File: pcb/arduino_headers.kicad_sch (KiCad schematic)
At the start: 4 parts, among them J4 Conn_01x08_Pin, J5 Conn_01x10_Pin, J6 Conn_01x06_Pin, J7 Conn_01x08_Pin

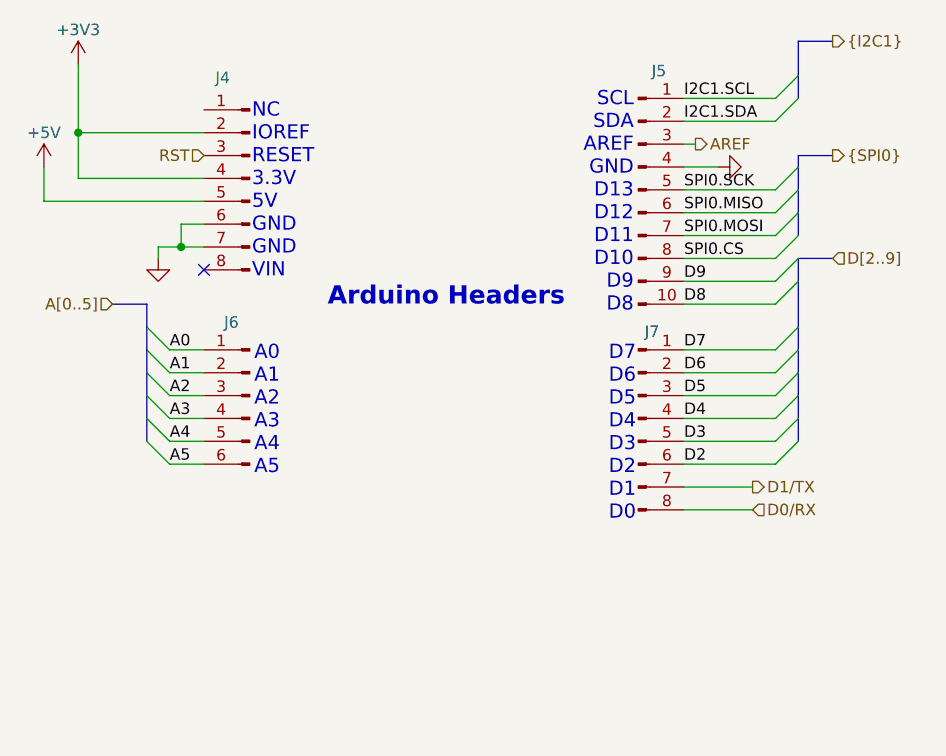
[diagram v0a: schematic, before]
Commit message: Added gerbers, added 2x3 Arduino header.
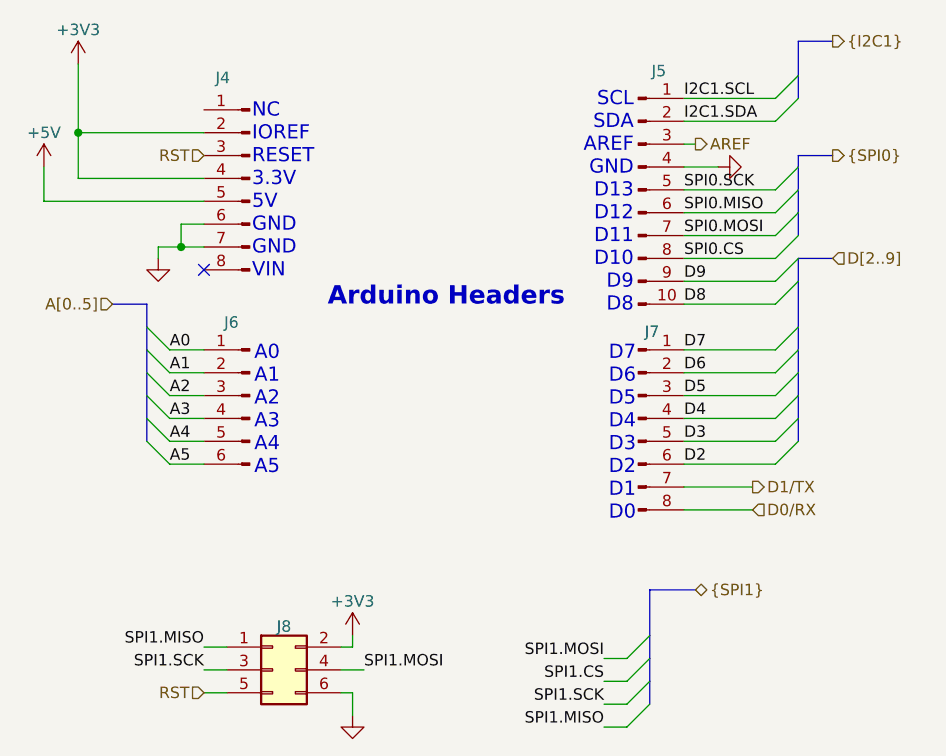
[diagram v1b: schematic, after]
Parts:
- added J8: Conn_02x03_Odd_Even, Connector_PinSocket_2.54mm:PinSocket_2x03_P2.54mm_Vertical, symbol Connector_Generic:Conn_02x03_Odd_Even
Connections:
- net +3V3: now also J8.2 (Pin_2)
- net GND: now also J8.6 (Pin_6)
- net RST: now also J8.5 (Pin_5)
- new net SPI1.MISO: J8.1 (Pin_1)
- new net SPI1.MOSI: J8.4 (Pin_4)
- new net SPI1.SCK: J8.3 (Pin_3)

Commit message: Added remaining part numbers, removed silk for holes, minor touchups
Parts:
- J4, J7: MPN (none) -> NPTC081KFXC-RC
- J5: MPN (none) -> NPTC101KFXC-RC
- J6: MPN (none) -> NPTC061KFXC-RC
- J8: footprint Connector_PinSocket_2.54mm:PinSocket_2x03_P2.54mm_Vertical -> Connector_PinHeader_2.54mm:PinHeader_2x03_P2.54mm_Vertical; MPN (none) -> 67997-206HLF
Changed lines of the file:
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@@
+			)
+		)
+		(property "MPN" "NPTC101KFXC-RC"
+			(at 177.8 82.55 0)
+			(effects
+				(font
+					(size 1.27 1.27)
+				)
+				(hide yes)
 			)
 		)
@@
 			)
 		)
+		(property "MPN" "NPTC081KFXC-RC"
+			(at 134.62 81.28 0)
+			(effects
+				(font
+					(size 1.27 1.27)
+				)
+				(hide yes)
+			)
+		)
 		(pin "2"
 		)
@@
 			)
 		)
+		(property "MPN" "NPTC061KFXC-RC"
+			(at 134.62 105.41 0)
+			(effects
+				(font
+					(size 1.27 1.27)
+				)
+				(hide yes)
+			)
+		)
 		(pin "6"
 		)
@@
 			)
 		)
-		(property "Footprint" "Connector_PinSocket_2.54mm:PinSocket_2x03_P2.54mm_Vertical"
+		(property "Footprint" "Connector_PinHeader_2.54mm:PinHeader_2x03_P2.54mm_Vertical"
 			(at 137.16 135.89 0)
 			(effects
@@
 			)
 		)
+		(property "MPN" "67997-206HLF"
+			(at 137.16 135.89 0)
+			(effects
+				(font
+					(size 1.27 1.27)
+				)
+				(hide yes)
+			)
+		)
 		(pin "1"
 		)
@@
 			(at 177.8 107.95 0)
 			(effects
+				(font
+					(size 1.27 1.27)
+				)
+				(hide yes)
+			)
+		)
+		(property "MPN" "NPTC081KFXC-RC"
+			(at 177.8 107.95 0)
+			(effects

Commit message: R0.1 released
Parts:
- renumbered J4 to J5, J5 to J6, J6 to J7, J7 to J8, J8 to J9
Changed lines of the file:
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@@
 		(on_board yes)
 		(dnp no)
-		(property "Reference" "J5"
+		(property "Reference" "J6"
 			(at 180.086 69.342 0)
 			(effects
@@
 			(project "blocky_breakout_pcb"
 				(path "/deaf739e-0e27-4f2f-890a-6dd284a38e9f/7c88a4ba-9535-4e16-9d9d-21b16df8d31a"
-					(reference "J5")
+					(reference "J6")
 					(unit 1)
 				)
@@
 		(on_board yes)
 		(dnp no)
-		(property "Reference" "#PWR048"
+		(property "Reference" "#PWR055"
 			(at 111.76 83.82 0)
 			(effects
@@
 			(project ""
 				(path "/deaf739e-0e27-4f2f-890a-6dd284a38e9f/7c88a4ba-9535-4e16-9d9d-21b16df8d31a"
-					(reference "#PWR048")
+					(reference "#PWR055")
 					(unit 1)
 				)
@@
 		(dnp no)
 		(fields_autoplaced yes)
-		(property "Reference" "#PWR067"
+		(property "Reference" "#PWR059"
 			(at 146.05 147.32 0)
 			(effects
@@
 			(project "blocky_breakout_pcb"
 				(path "/deaf739e-0e27-4f2f-890a-6dd284a38e9f/7c88a4ba-9535-4e16-9d9d-21b16df8d31a"
-					(reference "#PWR067")
+					(reference "#PWR059")
 					(unit 1)
 				)
@@
 		(on_board yes)
 		(dnp no)
-		(property "Reference" "J4"
+		(property "Reference" "J5"
 			(at 130.81 70.104 0)
 			(effects
@@
 			(project "blocky_breakout_pcb"
 				(path "/deaf739e-0e27-4f2f-890a-6dd284a38e9f/7c88a4ba-9535-4e16-9d9d-21b16df8d31a"
-					(reference "J4")
+					(reference "J5")
 					(unit 1)
 				)
@@
 		(dnp no)
 		(fields_autoplaced yes)
-		(property "Reference" "#PWR049"
+		(property "Reference" "#PWR056"
 			(at 193.04 80.01 0)
 			(effects
@@
 			(project "blocky_breakout_pcb"
 				(path "/deaf739e-0e27-4f2f-890a-6dd284a38e9f/7c88a4ba-9535-4e16-9d9d-21b16df8d31a"
-					(reference "#PWR049")
+					(reference "#PWR056")
 					(unit 1)
 				)
@@
 		(on_board yes)
 		(dnp no)
-		(property "Reference" "J6"
+		(property "Reference" "J7"
 			(at 132.588 97.282 0)
 			(effects
@@
 			(project "blocky_breakout_pcb"
 				(path "/deaf739e-0e27-4f2f-890a-6dd284a38e9f/7c88a4ba-9535-4e16-9d9d-21b16df8d31a"
-					(reference "J6")
+					(reference "J7")
 					(unit 1)
 				)
@@
 		(on_board yes)
 		(dnp no)
-		(property "Reference" "J8"
+		(property "Reference" "J9"
 			(at 138.43 131.064 0)
 			(effects
@@
 			(project ""
 				(path "/deaf739e-0e27-4f2f-890a-6dd284a38e9f/7c88a4ba-9535-4e16-9d9d-21b16df8d31a"
-					(reference "J8")
+					(reference "J9")
 					(unit 1)
 				)
@@
 		(on_board yes)
 		(dnp no)
-		(property "Reference" "J7"
+		(property "Reference" "J8"
 			(at 179.324 98.298 0)
 			(effects
@@
 			(project "blocky_breakout_pcb"
 				(path "/deaf739e-0e27-4f2f-890a-6dd284a38e9f/7c88a4ba-9535-4e16-9d9d-21b16df8d31a"
-					(reference "J7")
+					(reference "J8")
 					(unit 1)
 				)
@@
 		(on_board yes)
 		(dnp no)
-		(property "Reference" "#PWR047"
+		(property "Reference" "#PWR054"
 			(at 115.57 72.39 0)
 			(effects
@@
 			(project "blocky_breakout_pcb"
 				(path "/deaf739e-0e27-4f2f-890a-6dd284a38e9f/7c88a4ba-9535-4e16-9d9d-21b16df8d31a"
-					(reference "#PWR047")
+					(reference "#PWR054")
 					(unit 1)
 				)
@@
 		(dnp no)
 		(fields_autoplaced yes)
-		(property "Reference" "#PWR050"
+		(property "Reference" "#PWR057"
 			(at 124.46 96.52 0)
 			(effects
@@
 			(project ""
 				(path "/deaf739e-0e27-4f2f-890a-6dd284a38e9f/7c88a4ba-9535-4e16-9d9d-21b16df8d31a"
-					(reference "#PWR050")
+					(reference "#PWR057")
 					(unit 1)
 				)
@@
 		(on_board yes)
 		(dnp no)
-		(property "Reference" "#PWR068"
+		(property "Reference" "#PWR058"
 			(at 146.05 135.89 0)
 			(effects
@@
 			(project "blocky_breakout_pcb"
 				(path "/deaf739e-0e27-4f2f-890a-6dd284a38e9f/7c88a4ba-9535-4e16-9d9d-21b16df8d31a"
-					(reference "#PWR068")
-					(unit 1)
-				)
+					(reference "#PWR058")
+					(unit 1)
+				)
